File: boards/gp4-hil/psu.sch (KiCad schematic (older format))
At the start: 16 parts, among them K1 CONN_3_PWROUT, U3 LTC3374-QFN

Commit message: Added load switches for DUT_VDDx rails
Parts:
- added C125, C126, C127, C128: 22 uF, symbol C
- added C129: 2.2 uF, symbol C
- added C130: 10 uF 16V, symbol C
- added C131, C132, C133, C137, C138, C139: 4.7 uF, symbol C
- added C134, C135, C136, C140, C141, C142: 0.47 uF, symbol C
- added D20: CDBQR0130L, symbol D_Schottky
- added L10, L11, L7, L9: 2.2 uH 3.7A, symbol INDUCTOR_PWROUT
- added L12: 10 uH, symbol INDUCTOR_PWROUT
- added L8: 600R, symbol INDUCTOR_PWROUT
- added R104: 232K, symbol R
- added R105: 464K, symbol R
- added R106: 806K, symbol R
- added R107: 649K, symbol R
- added R108, R110: 1.02M, symbol R
- added R109: 475K, symbol R
- added R111: 324K, symbol R
- added R112: 24K, symbol R
- added R113: 4.7K 1%, symbol R
- added U1: MIC2288-DFN, symbol MIC2288-DFN
- added U20, U21, U22, U23, U24, U4: SIP32408, symbol SIP32408
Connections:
- net 1V2: now also C125.1, L7.1, R104.1
- net 1V8: now also C126.1, C133.1, C139.1, L9.1, R106.1, U21.1 (IN), U24.1 (IN)
- net 2V5: now also C127.1, C132.1, C138.1, L10.1, R108.1, U20.1 (IN), U23.1 (IN)
- net 3V3: now also C128.1, C131.1, C137.1, L11.1, R110.1, U22.1 (IN), U4.1 (IN)
- net 5V0: now also U3.18 (EN6), U3.19 (EN5), U3.21 (VIN5), U3.24 (VIN6), U3.27 (VIN7), U3.30 (VIN8), U3.32 (EN8), U3.33 (EN7), C129.2, L12.2, L8.1, U1.2 (VIN), U1.3 (EN)
- net 5V0_IN: now also L8.2
- net DUT_VDD1: now also C134.1, C135.1, C136.1, U20.4 (OUT), U21.4 (OUT), U4.4 (OUT)
- net DUT_VDD2: now also C140.1, C141.1, C142.1, U22.4 (OUT), U23.4 (OUT), U24.4 (OUT)
- net GND: now also C125.2, C126.2, C127.2, C128.2, C129.1, C130.2, C131.2, C132.2, C133.2, C134.2, C135.2, C136.2, C137.2, C138.2, C139.2, C140.2, C141.2, C142.2, R105.1, R107.1, R109.1, R111.1, R113.2, U1.4 (AGND), U1.8 (PGND), U1.PAD (GND), U20.2 (GND), U20.PAD (GND), U21.2 (GND), U21.PAD (GND), U22.2 (GND), U22.PAD (GND), U23.2 (GND), U23.PAD (GND), U24.2 (GND), U24.PAD (GND), U4.2 (GND), U4.PAD (GND)
- net FB_1V2: now reaches U3.20 (FB5)
- net FB_1V2: now also R104.2, R105.2
- net SW_1V2: now reaches U3.22 (SW5)
- net SW_1V2: now also L7.2
- net SW_1V8: now reaches U3.23 (SW6)
- net SW_1V8: now also L9.2
- net FB_1V8: now reaches U3.25 (FB6)
- net FB_1V8: now also R106.2, R107.2
- net FB_2V5: now reaches U3.26 (FB7)
- net FB_2V5: now also R108.2, R109.2
- net SW_2V5: now reaches U3.28 (SW7)
- net SW_2V5: now also L10.2
- net SW_3V3: now reaches U3.29 (SW8)
- net SW_3V3: now also L11.2
- net FB_3V3: now reaches U3.31 (FB8)
- net FB_3V3: now also R110.2, R111.2
- new net: R112.2, R113.1, U1.6 (FB)
- new net: D20.2 (A), L12.1, U1.7 (SW)
- new net DUT_VPP_RAW: C130.1, D20.1 (K), R112.1, U1.1 (OVP)
- new net VDD1_1V8_EN: U21.3 (EN)
- new net VDD1_2V5_EN: U20.3 (EN)
- new net VDD1_3V3_EN: U4.3 (EN)
- new net VDD2_1V8_EN: U24.3 (EN)
- new net VDD2_2V5_EN: U23.3 (EN)
- new net VDD2_3V3_EN: U22.3 (EN)
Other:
- note added: "FPGA and DUT power conversion"
- note added: "Load switching for DUT_VDDx"
- note added: "SMPS input caps"
- note added: "Vpp generation"
- note added: "vout = 1.24 * (R1 / 4700 + 1)\nR1 = 24k"
- note removed: "1V0 input caps"
- note removed: "TODO: Load switching for DUT_VDDx\nTODO: Load switching for VPP"
- note removed: "TODO: See if we can get low enough power to run off USB?"
- moved on the sheet: C116, C117, C118, C119, C120, C121, C123, C124, K1, U3E, U3F

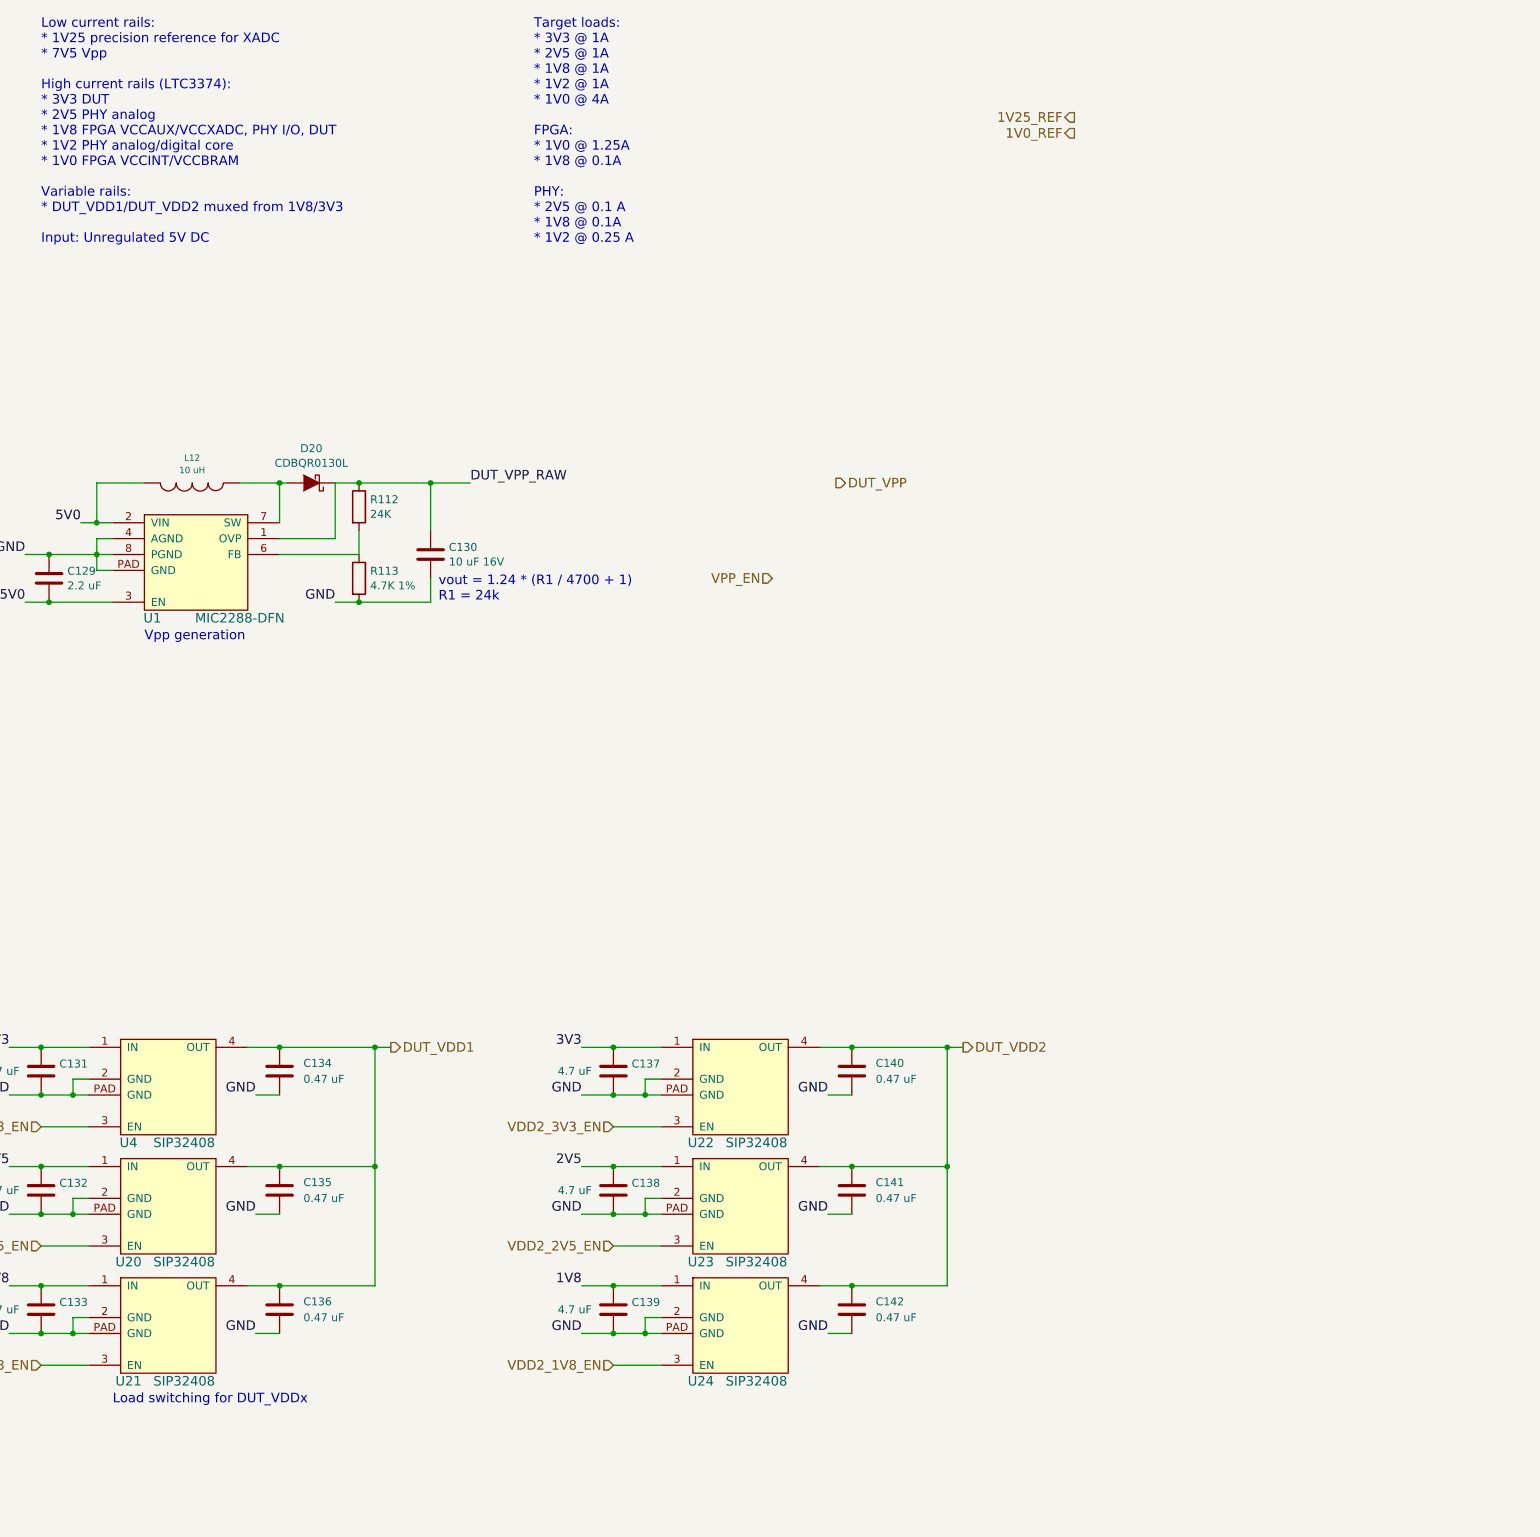
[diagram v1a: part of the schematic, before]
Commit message: Merged JTAG master stuff with Ethernet schematic page
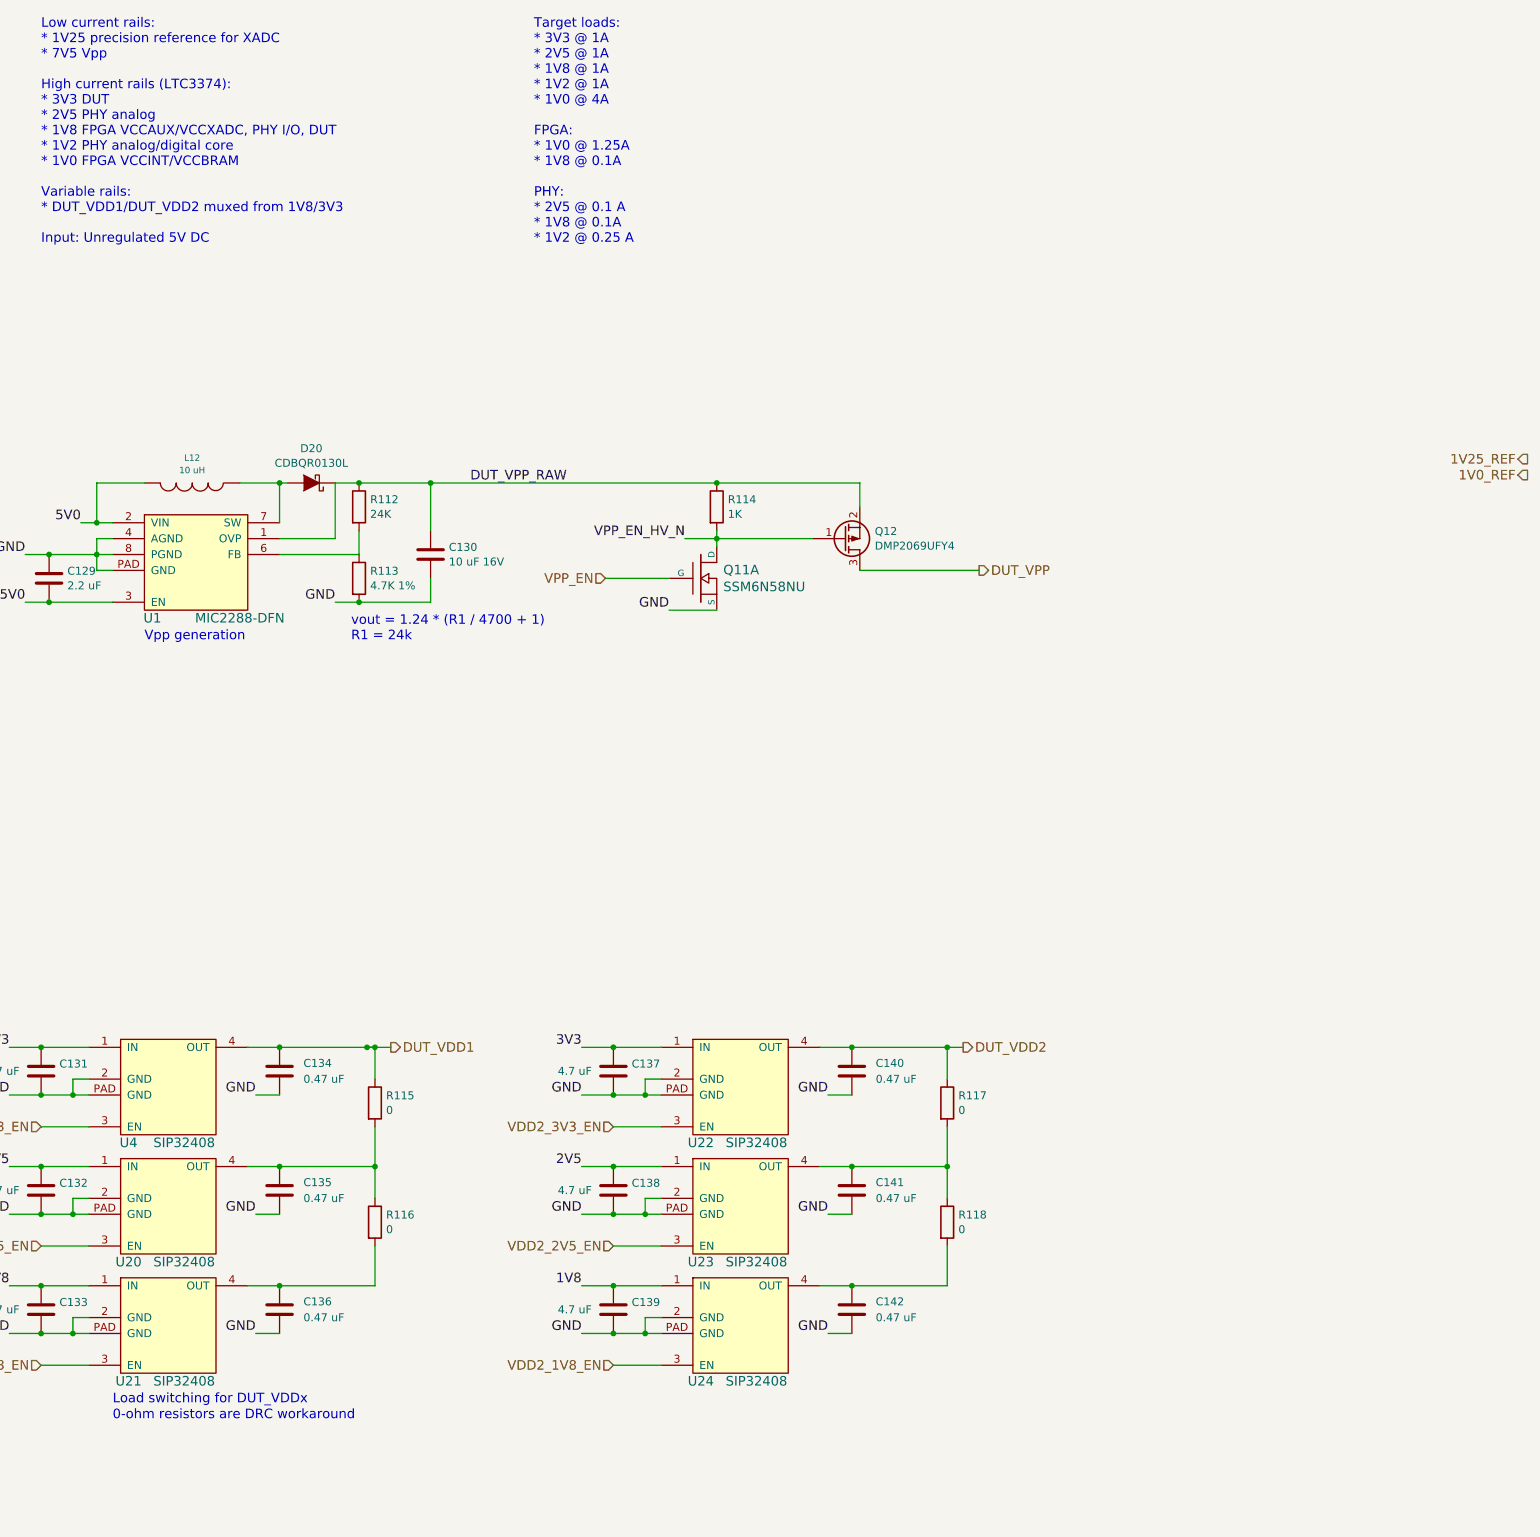
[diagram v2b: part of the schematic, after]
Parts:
- added Q11: SSM6N58NU, symbol SSM6N58NU_DUAL_NMOS
- added Q12: DMP2069UFY4, symbol Q_PMOS_GSD
- added R114: 1K, symbol R
- added R115, R116, R117, R118: 0, symbol R
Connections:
- net DUT_VDD1: now also R115.1; no longer C135.1, C136.1, U20.4 (OUT), U21.4 (OUT)
- net DUT_VDD2: now also R117.1; no longer C141.1, C142.1, U23.4 (OUT), U24.4 (OUT)
- net DUT_VPP: now also Q12.3 (D)
- net DUT_VPP_RAW: now also Q12.2 (S), R114.1
- net GND: now also Q11.S1 (S)
- net VPP_EN: now also Q11.G1 (G)
- new net: C136.1, R116.2, U21.4 (OUT)
- new net: C135.1, R115.2, R116.1, U20.4 (OUT)
- new net: C142.1, R118.2, U24.4 (OUT)
- new net: C141.1, R117.2, R118.1, U23.4 (OUT)
- new net VPP_EN_HV_N: Q11.D1 (D), Q12.1 (G), R114.2
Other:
- note added: "0-ohm resistors are DRC workaround"

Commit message: Wired up FPGA config pins, flash, etc
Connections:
- net 1V8: now also R100.2
- net 2V5: no longer R100.2
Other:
- note removed: "TODO: what rail to pull to?"
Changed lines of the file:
@@
 PSU_VTEMP
 Text Label 4050 1450 0    60   ~ 0
-2V5
-Text Notes 4050 1350 0    60   ~ 0
-TODO: what rail to pull to?
+1V8
 Text Notes 2100 2300 0    60   ~ 0
 TODO: VCC cap

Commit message: Added lots of analog I/O stuff
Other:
- note added: "Low current rails:\n* 7V5 Vpp\n\nHigh current rails (LTC3374):\n* 3V3 DUT\n* 2V5 PHY analog\n* 1V8 FPGA VCCAUX/VCCXADC, PHY I/O, DUT\n* 1V2 PHY analog/digital core\n* 1V0 FPGA VCCINT/VCCBRAM\n\nVariable rails:\n* DUT_VDD1/DUT_VDD2 muxed from 1V8/3V3\n\nInput: Unregulated 5V DC"
- note removed: "Low current rails:\n* 1V25 precision reference for XADC\n* 7V5 Vpp\n\nHigh current rails (LTC3374):\n* 3V3 DUT\n* 2V5 PHY analog\n* 1V8 FPGA VCCAUX/VCCXADC, PHY I/O, DUT\n* 1V2 PHY analog/digital core\n* 1V0 FPGA VCCINT/VCCBRAM\n\nVariable rails:\n* DUT_VDD1/DUT_VDD2 muxed from 1V8/3V3\n\nInput: Unregulated 5V DC"
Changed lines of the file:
@@
 $EndDescr
 Text Notes 7200 2500 0    60   ~ 0
-Low current rails:\n* 1V25 precision reference for XADC\n* 7V5 Vpp\n\nHigh current rails (LTC3374):\n* 3V3 DUT\n* 2V5 PHY analog\n* 1V8 FPGA VCCAUX/VCCXADC, PHY I/O, DUT\n* 1V2 PHY analog/digital core\n* 1V0 FPGA VCCINT/VCCBRAM\n\nVariable rails:\n* DUT_VDD1/DUT_VDD2 muxed from 1V8/3V3\n\nInput: Unregulated 5V DC
+Low current rails:\n* 7V5 Vpp\n\nHigh current rails (LTC3374):\n* 3V3 DUT\n* 2V5 PHY analog\n* 1V8 FPGA VCCAUX/VCCXADC, PHY I/O, DUT\n* 1V2 PHY analog/digital core\n* 1V0 FPGA VCCINT/VCCBRAM\n\nVariable rails:\n* DUT_VDD1/DUT_VDD2 muxed from 1V8/3V3\n\nInput: Unregulated 5V DC
 $Comp
 L LTC3374-QFN U3
@@
 Text HLabel 4350 1750 2    60   Output ~ 0
 PSU_PGOOD
-Text HLabel 16550 3850 0    60   Output ~ 0
-1V25_REF
-Text HLabel 16550 3950 0    60   Output ~ 0
-1V0_REF
 Text Notes 7650 9800 0    60   ~ 0
 Load switching for DUT_VDDx

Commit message: Added FPGA core clock, GPIO indicator LEDs, expansion header, lots of test points
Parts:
- added C171: 4.7 uF, symbol C
- added C172: 0.47 uF, symbol C
- added TP24, TP25, TP26, TP27, TP28, TP29, TP30, TP31, TP32: TESTPOINT, symbol CONN_01X01
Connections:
- net 1V0: now also TP25.1 (P1)
- net 1V2: now also TP26.1 (P1)
- net 1V8: now also TP27.1 (P1)
- net 2V5: now also TP28.1 (P1)
- net 3V3: now also TP29.1 (P1)
- net 5V0: now also C171.1, C172.1
- net DUT_VPP_RAW: now also TP30.1 (P1)
- net GND: now also C171.2, C172.2, TP24.1 (P1)
- net PSU_PGOOD: now also TP31.1 (P1)
- net PSU_VTEMP: now also TP32.1 (P1)
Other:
- note removed: "TODO: VCC cap"
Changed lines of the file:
@@
 Text HLabel 5250 4100 2    60   Output ~ 0
 1V0
-Text HLabel 1750 2050 0    60   Output ~ 0
+Text HLabel 900  2050 0    60   Output ~ 0
 GND
 Text HLabel 9400 7550 2    60   Output ~ 0
@@
 Text Notes 10300 2500 0    60   ~ 0
 Target loads:\n* 3V3 @ 1A\n* 2V5 @ 1A\n* 1V8 @ 1A\n* 1V2 @ 1A\n* 1V0 @ 4A\n\nFPGA:\n* 1V0 @ 1.25A\n* 1V8 @ 0.1A\n\nPHY:\n* 2V5 @ 0.1 A\n* 1V8 @ 0.1A\n* 1V2 @ 0.25 A
-Text Label 1750 1650 2    60   ~ 0
+Text Label 900  1650 2    60   ~ 0
 5V0
 $Comp
@@
 Text Label 4050 1450 0    60   ~ 0
 1V8
-Text Notes 2100 2300 0    60   ~ 0
-TODO: VCC cap
 Text Label 3550 3800 0    60   ~ 0
 5V0
@@
 	1    0    0    -1
 $EndComp
-Text Label 9900 4000 0    60   ~ 0
-DUT_VPP_RAW
 Text Label 7100 4450 2    60   ~ 0
 GND
@@
 	2250 15100 2050 15100
 Wire Wire Line
-	1750 1650 1900 1650
-Wire Wire Line
-	1750 2050 1900 2050
+	900  1650 1900 1650
+Wire Wire Line
+	900  2050 1900 2050
 Wire Wire Line
 	3200 1750 4350 1750
@@
 	9050 4350 9050 4000
 Wire Wire Line
-	9050 4000 12350 4000
+	9050 4000 12600 4000
 Wire Wire Line
 	8700 4450 9200 4450
@@
 Wire Wire Line
 	12900 7550 12900 7750
+$Comp
+L C C172
+U 1 1 5753265C
+P 1600 1800
+F 0 "C172" H 1715 1846 50  0000 L CNN
+F 1 "0.47 uF" H 1715 1754 50  0000 L CNN
+F 2 "" H 1638 1650 30  0000 C CNN
+F 3 "" H 1600 1800 60  0000 C CNN
+	1    1600 1800
+	1    0    0    -1
+$EndComp
+$Comp
+L C C171
+U 1 1 57532AC4
+P 1050 1800
+F 0 "C171" H 1165 1846 50  0000 L CNN
+F 1 "4.7 uF" H 1165 1754 50  0000 L CNN
+F 2 "" H 1088 1650 30  0000 C CNN
+F 3 "" H 1050 1800 60  0000 C CNN
+	1    1050 1800
+	1    0    0    -1
+$EndComp
+Connection ~ 1600 1650
+Connection ~ 1050 1650
+Wire Wire Line
+	1050 1950 1050 2050
+Connection ~ 1050 2050
+Wire Wire Line
+	1600 1950 1600 2050
+Connection ~ 1600 2050
+Text HLabel 12600 4000 2    60   Output ~ 0
+DUT_VPP_RAW
+Connection ~ 12350 4000
+$Comp
+L CONN_01X01 TP24
+U 1 1 57555F4E
+P 21500 1350
+F 0 "TP24" H 21578 1388 50  0000 L CNN
+F 1 "TESTPOINT" H 21578 1296 50  0000 L CNN
+F 2 "" H 21500 1350 60  0000 C CNN
+F 3 "" H 21500 1350 60  0000 C CNN
+	1    21500 1350
+	1    0    0    -1
+$EndComp
+Text Label 21050 1350 2    60   ~ 0
+GND
+Wire Wire Line
+	21300 1350 21050 1350
+$Comp
+L CONN_01X01 TP25
+U 1 1 575560E7
+P 21500 1650
+F 0 "TP25" H 21578 1688 50  0000 L CNN
+F 1 "TESTPOINT" H 21578 1596 50  0000 L CNN
+F 2 "" H 21500 1650 60  0000 C CNN
+F 3 "" H 21500 1650 60  0000 C CNN
+	1    21500 1650
+	1    0    0    -1
+$EndComp
+Text Label 21050 1650 2    60   ~ 0
+1V0
+Wire Wire Line
+	21300 1650 21050 1650
+$Comp
+L CONN_01X01 TP26
+U 1 1 57556285
+P 21500 1950
+F 0 "TP26" H 21578 1988 50  0000 L CNN
+F 1 "TESTPOINT" H 21578 1896 50  0000 L CNN
+F 2 "" H 21500 1950 60  0000 C CNN
+F 3 "" H 21500 1950 60  0000 C CNN
+	1    21500 1950
+	1    0    0    -1
+$EndComp
+Text Label 21050 1950 2    60   ~ 0
+1V2
+Wire Wire Line
+	21300 1950 21050 1950
+$Comp
+L CONN_01X01 TP27
+U 1 1 5755650C
+P 21500 2250
+F 0 "TP27" H 21578 2288 50  0000 L CNN
+F 1 "TESTPOINT" H 21578 2196 50  0000 L CNN
+F 2 "" H 21500 2250 60  0000 C CNN
+F 3 "" H 21500 2250 60  0000 C CNN
+	1    21500 2250
+	1    0    0    -1
+$EndComp
+Text Label 21050 2250 2    60   ~ 0
+1V8
+Wire Wire Line
+	21300 2250 21050 2250
+$Comp
+L CONN_01X01 TP28
+U 1 1 5755670D
+P 21500 2550
+F 0 "TP28" H 21578 2588 50  0000 L CNN
+F 1 "TESTPOINT" H 21578 2496 50  0000 L CNN
+F 2 "" H 21500 2550 60  0000 C CNN
+F 3 "" H 21500 2550 60  0000 C CNN
+	1    21500 2550
+	1    0    0    -1
+$EndComp
+Text Label 21050 2550 2    60   ~ 0
+2V5
+Wire Wire Line
+	21300 2550 21050 2550
+$Comp
+L CONN_01X01 TP29
+U 1 1 575569AA
+P 21500 2850
+F 0 "TP29" H 21578 2888 50  0000 L CNN
+F 1 "TESTPOINT" H 21578 2796 50  0000 L CNN
+F 2 "" H 21500 2850 60  0000 C CNN
+F 3 "" H 21500 2850 60  0000 C CNN
+	1    21500 2850
+	1    0    0    -1
+$EndComp
+Text Label 21050 2850 2    60   ~ 0
+3V3
+Wire Wire Line
+	21300 2850 21050 2850
+$Comp
+L CONN_01X01 TP30
+U 1 1 57557165
+P 21500 3150
+F 0 "TP30" H 21578 3188 50  0000 L CNN
+F 1 "TESTPOINT" H 21578 3096 50  0000 L CNN
+F 2 "" H 21500 3150 60  0000 C CNN
+F 3 "" H 21500 3150 60  0000 C CNN
+	1    21500 3150
+	1    0    0    -1
+$EndComp
+Text Label 21050 3150 2    60   ~ 0
+DUT_VPP_RAW
+Wire Wire Line
+	21300 3150 21050 3150
+$Comp
+L CONN_01X01 TP31
+U 1 1 57557CCF
+P 21500 3450
+F 0 "TP31" H 21578 3488 50  0000 L CNN
+F 1 "TESTPOINT" H 21578 3396 50  0000 L CNN
+F 2 "" H 21500 3450 60  0000 C CNN
+F 3 "" H 21500 3450 60  0000 C CNN
+	1    21500 3450
+	1    0    0    -1
+$EndComp
+Text Label 21050 3450 2    60   ~ 0
+PSU_PGOOD
+Wire Wire Line
+	21300 3450 21050 3450
+$Comp
+L CONN_01X01 TP32
+U 1 1 57558505
+P 21500 3750
+F 0 "TP32" H 21578 3788 50  0000 L CNN
+F 1 "TESTPOINT" H 21578 3696 50  0000 L CNN
+F 2 "" H 21500 3750 60  0000 C CNN
+F 3 "" H 21500 3750 60  0000 C CNN
+	1    21500 3750
+	1    0    0    -1
+$EndComp
+Text Label 21050 3750 2    60   ~ 0
+PSU_VTEMP
+Wire Wire Line
+	21300 3750 21050 3750
 $EndSCHEMATC
